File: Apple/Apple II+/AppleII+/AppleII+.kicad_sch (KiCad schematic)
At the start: 0 parts

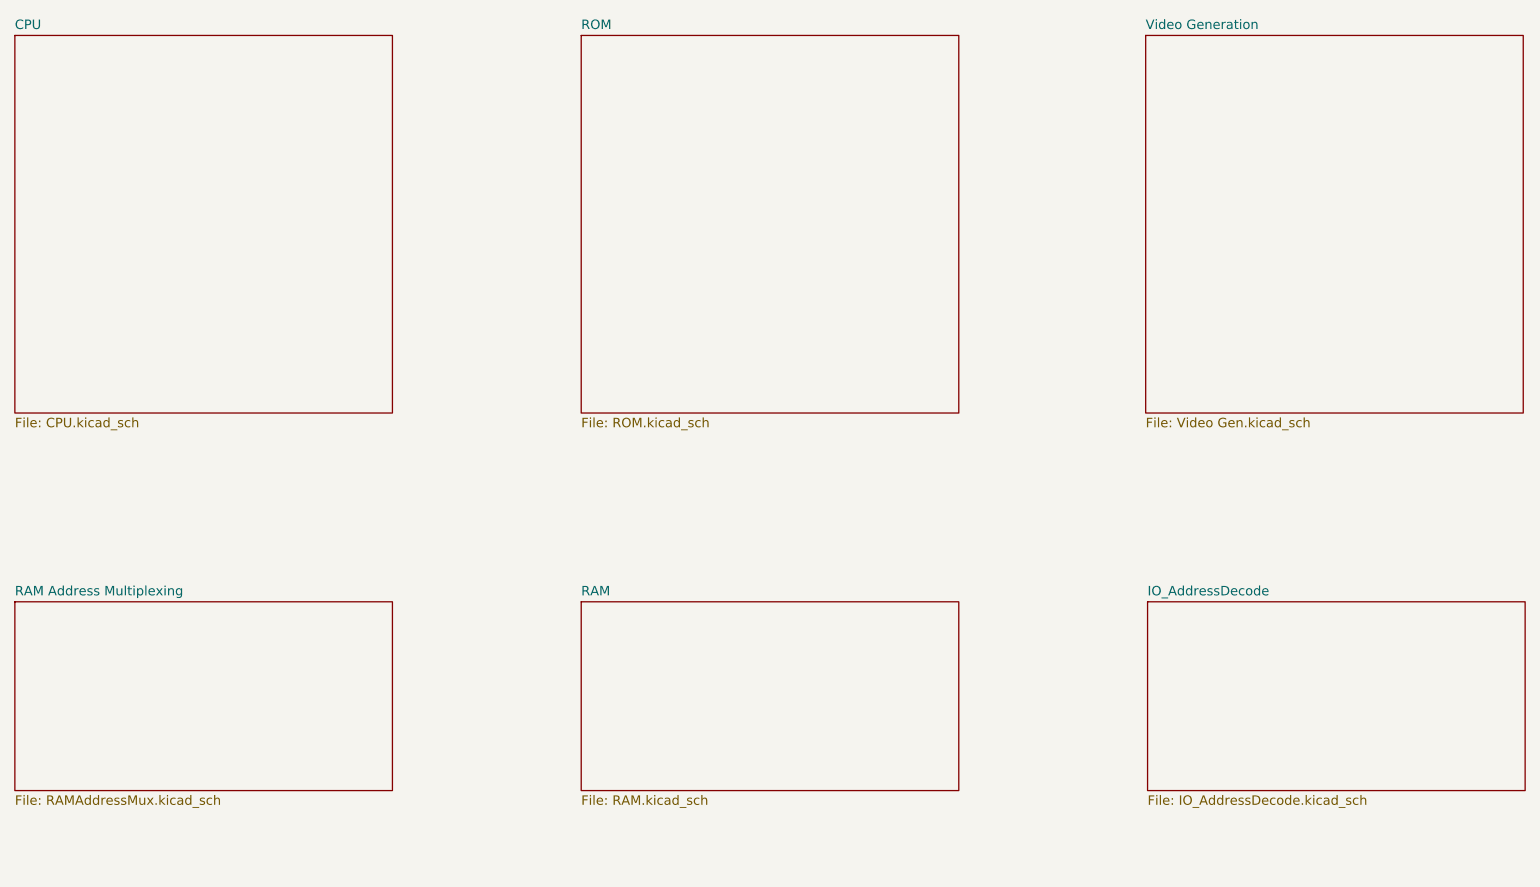
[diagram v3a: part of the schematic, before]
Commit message: Started moving Global labels to Hierarchical and Local labels
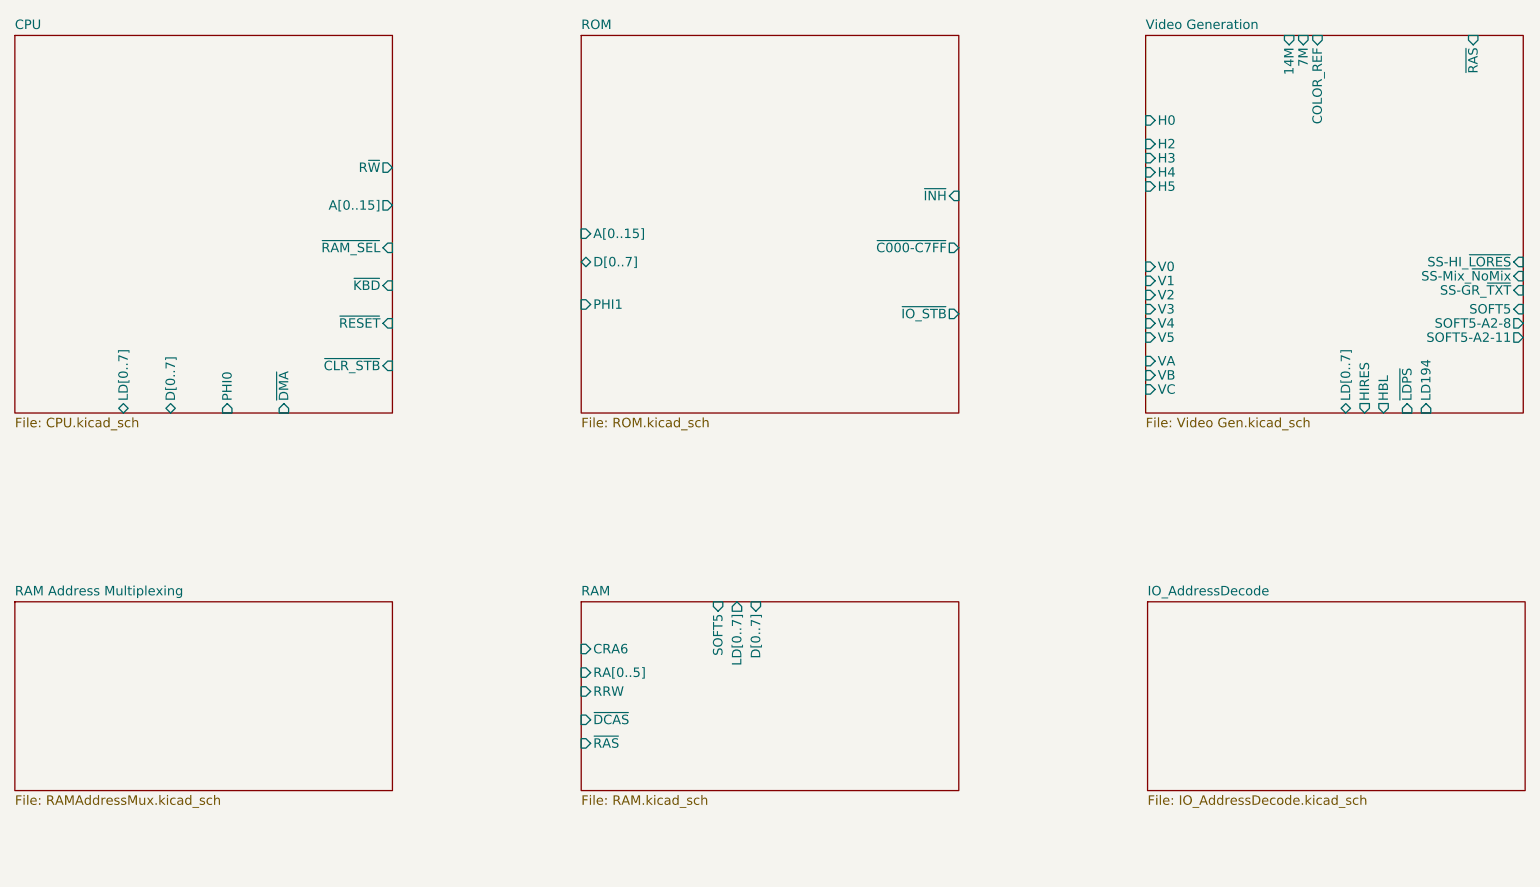
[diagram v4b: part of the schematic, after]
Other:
- sheet CPU ports: added A[0..15], D[0..7], LD[0..7], PHI0, R~{W}, ~{CLR_STB}, ~{DMA}, ~{KBD}, ~{RAM_SEL}, ~{RESET}; removed none
- sheet RAM ports: added CRA6, D[0..7], LD[0..7], RA[0..5], RRW, SOFT5, ~{DCAS}, ~{RAS}; removed none
- sheet ROM ports: added A[0..15], D[0..7], PHI1, ~{C000-C7FF}, ~{INH}, ~{IO_STB}; removed none
- sheet Video Generation ports: added 14M, 7M, COLOR_REF, H0, H2, H3, H4, H5, HBL, HIRES, LD194, LD[0..7], SOFT5, SOFT5-A2-11, SOFT5-A2-8, SS-GR_~{TXT}, SS-HI_~{LORES}, SS-Mix_~{NoMix}, V0, V1, V2, V3, V4, V5, VA, VB, VC, ~{LDPS}, ~{RAS}; removed none
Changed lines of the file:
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@@
       (effects (font (size 1.27 1.27)) (justify left top))
+    )
+    (pin "R~{W}" output (at 76.2 43.18 0)
+      (effects (font (size 1.27 1.27)) (justify right))
+    )
+    (pin "A[0..15]" output (at 76.2 48.26 0)
+      (effects (font (size 1.27 1.27)) (justify right))
+    )
+    (pin "~{RAM_SEL}" input (at 76.2 53.975 0)
+      (effects (font (size 1.27 1.27)) (justify right))
+    )
+    (pin "~{KBD}" input (at 76.2 59.055 0)
+      (effects (font (size 1.27 1.27)) (justify right))
+    )
+    (pin "~{RESET}" input (at 76.2 64.135 0)
+      (effects (font (size 1.27 1.27)) (justify right))
+    )
+    (pin "~{CLR_STB}" input (at 76.2 69.85 0)
+      (effects (font (size 1.27 1.27)) (justify right))
+    )
+    (pin "~{DMA}" input (at 61.595 76.2 270)
+      (effects (font (size 1.27 1.27)) (justify left))
+    )
+    (pin "PHI0" input (at 53.975 76.2 270)
+      (effects (font (size 1.27 1.27)) (justify left))
+    )
+    (pin "D[0..7]" bidirectional (at 46.355 76.2 270)
+      (effects (font (size 1.27 1.27)) (justify left))
+    )
+    (pin "LD[0..7]" bidirectional (at 40.005 76.2 270)
+      (effects (font (size 1.27 1.27)) (justify left))
     )
     (instances
@@
       (effects (font (size 1.27 1.27)) (justify left top))
     )
+    (pin "~{INH}" input (at 152.4 46.99 0)
+      (effects (font (size 1.27 1.27)) (justify right))
+    )
+    (pin "~{C000-C7FF}" output (at 152.4 53.975 0)
+      (effects (font (size 1.27 1.27)) (justify right))
+    )
+    (pin "~{IO_STB}" output (at 152.4 62.865 0)
+      (effects (font (size 1.27 1.27)) (justify right))
+    )
+    (pin "D[0..7]" bidirectional (at 101.6 55.88 180)
+      (effects (font (size 1.27 1.27)) (justify left))
+    )
+    (pin "A[0..15]" input (at 101.6 52.07 180)
+      (effects (font (size 1.27 1.27)) (justify left))
+    )
+    (pin "PHI1" input (at 101.6 61.595 180)
+      (effects (font (size 1.27 1.27)) (justify left))
+    )
     (instances
       (project "AppleII+"
@@
       (effects (font (size 1.27 1.27)) (justify left top))
     )
+    (pin "LD[0..7]" output (at 122.555 101.6 90)
+      (effects (font (size 1.27 1.27)) (justify right))
+    )
+    (pin "CRA6" input (at 101.6 107.95 180)
+      (effects (font (size 1.27 1.27)) (justify left))
+    )
+    (pin "RA[0..5]" input (at 101.6 111.125 180)
+      (effects (font (size 1.27 1.27)) (justify left))
+    )
+    (pin "RRW" input (at 101.6 113.665 180)
+      (effects (font (size 1.27 1.27)) (justify left))
+    )
+    (pin "D[0..7]" input (at 125.095 101.6 90)
+      (effects (font (size 1.27 1.27)) (justify right))
+    )
+    (pin "~{DCAS}" input (at 101.6 117.475 180)
+      (effects (font (size 1.27 1.27)) (justify left))
+    )
+    (pin "~{RAS}" input (at 101.6 120.65 180)
+      (effects (font (size 1.27 1.27)) (justify left))
+    )
+    (pin "SOFT5" input (at 120.015 101.6 90)
+      (effects (font (size 1.27 1.27)) (justify right))
+    )
     (instances
       (project "AppleII+"
@@
       (effects (font (size 1.27 1.27)) (justify left top))
     )
-    (instances
+    (pin "V3" input (at 177.546 62.23 180)
+      (effects (font (size 1.27 1.27)) (justify left))
+    )
+    (pin "V4" input (at 177.546 64.135 180)
+      (effects (font (size 1.27 1.27)) (justify left))
+    )
+    (pin "COLOR_REF" input (at 200.66 25.4 90)
+      (effects (font (size 1.27 1.27)) (justify right))
+    )
+    (pin "H3" input (at 177.546 41.91 180)
+      (effects (font (size 1.27 1.27)) (justify left))
+    )
+    (pin "V5" input (at 177.546 66.04 180)
+      (effects (font (size 1.27 1.27)) (justify left))
+    )
+    (pin "H4" input (at 177.546 43.815 180)
+      (effects (font (size 1.27 1.27)) (justify left))
+    )
+    (pin "H5" input (at 177.546 45.72 180)
+      (effects (font (size 1.27 1.27)) (justify left))
+    )
+    (pin "V1" input (at 177.546 58.42 180)
+      (effects (font (size 1.27 1.27)) (justify left))
+    )
+    (pin "V0" input (at 177.546 56.515 180)
+      (effects (font (size 1.27 1.27)) (justify left))
+    )
+    (pin "VC" input (at 177.546 73.025 180)
+      (effects (font (size 1.27 1.27)) (justify left))
+    )
+    (pin "V2" input (at 177.546 60.325 180)
+      (effects (font (size 1.27 1.27)) (justify left))
+    )
+    (pin "VB" input (at 177.546 71.12 180)
+      (effects (font (size 1.27 1.27)) (justify left))
+    )
+    (pin "VA" input (at 177.546 69.215 180)
+      (effects (font (size 1.27 1.27)) (justify left))
+    )
+    (pin "SOFT5-A2-11" output (at 228.346 66.04 0)
+      (effects (font (size 1.27 1.27)) (justify right))
+    )
+    (pin "SOFT5-A2-8" output (at 228.346 64.135 0)
+      (effects (font (size 1.27 1.27)) (justify right))
+    )
+    (pin "HIRES" output (at 207.01 76.2 270)
+      (effects (font (size 1.27 1.27)) (justify left))
+    )
+    (pin "HBL" output (at 209.55 76.2 270)
+      (effects (font (size 1.27 1.27)) (justify left))
+    )
+    (pin "LD[0..7]" bidirectional (at 204.47 76.2 270)
+      (effects (font (size 1.27 1.27)) (justify left))
+    )
+    (pin "14M" input (at 196.85 25.4 90)
+      (effects (font (size 1.27 1.27)) (justify right))
+    )
+    (pin "7M" input (at 198.755 25.4 90)
+      (effects (font (size 1.27 1.27)) (justify right))
+    )
+    (pin "~{LDPS}" input (at 212.725 76.2 270)
+      (effects (font (size 1.27 1.27)) (justify left))
+    )
+    (pin "LD194" input (at 215.265 76.2 270)
+      (effects (font (size 1.27 1.27)) (justify left))
+    )
+    (pin "SOFT5" input (at 228.346 62.23 0)
+      (effects (font (size 1.27 1.27)) (justify right))
+    )
+    (pin "H0" input (at 177.546 36.83 180)
+      (effects (font (size 1.27 1.27)) (justify left))
+    )
+    (pin "H2" input (at 177.546 40.005 180)
+      (effects (font (size 1.27 1.27)) (justify left))
+    )
+    (pin "SS-GR_~{TXT}" input (at 228.346 59.69 0)
+      (effects (font (size 1.27 1.27)) (justify right))
+    )
+    (pin "SS-Mix_~{NoMix}" input (at 228.346 57.785 0)
+      (effects (font (size 1.27 1.27)) (justify right))
+    )
+    (pin "~{RAS}" input (at 221.615 25.4 90)
+      (effects (font (size 1.27 1.27)) (justify right))
+    )
+    (pin "SS-HI_~{LORES}" input (at 228.346 55.88 0)
+      (effects (font (size 1.27 1.27)) (justify right))
+    )
+    (instances

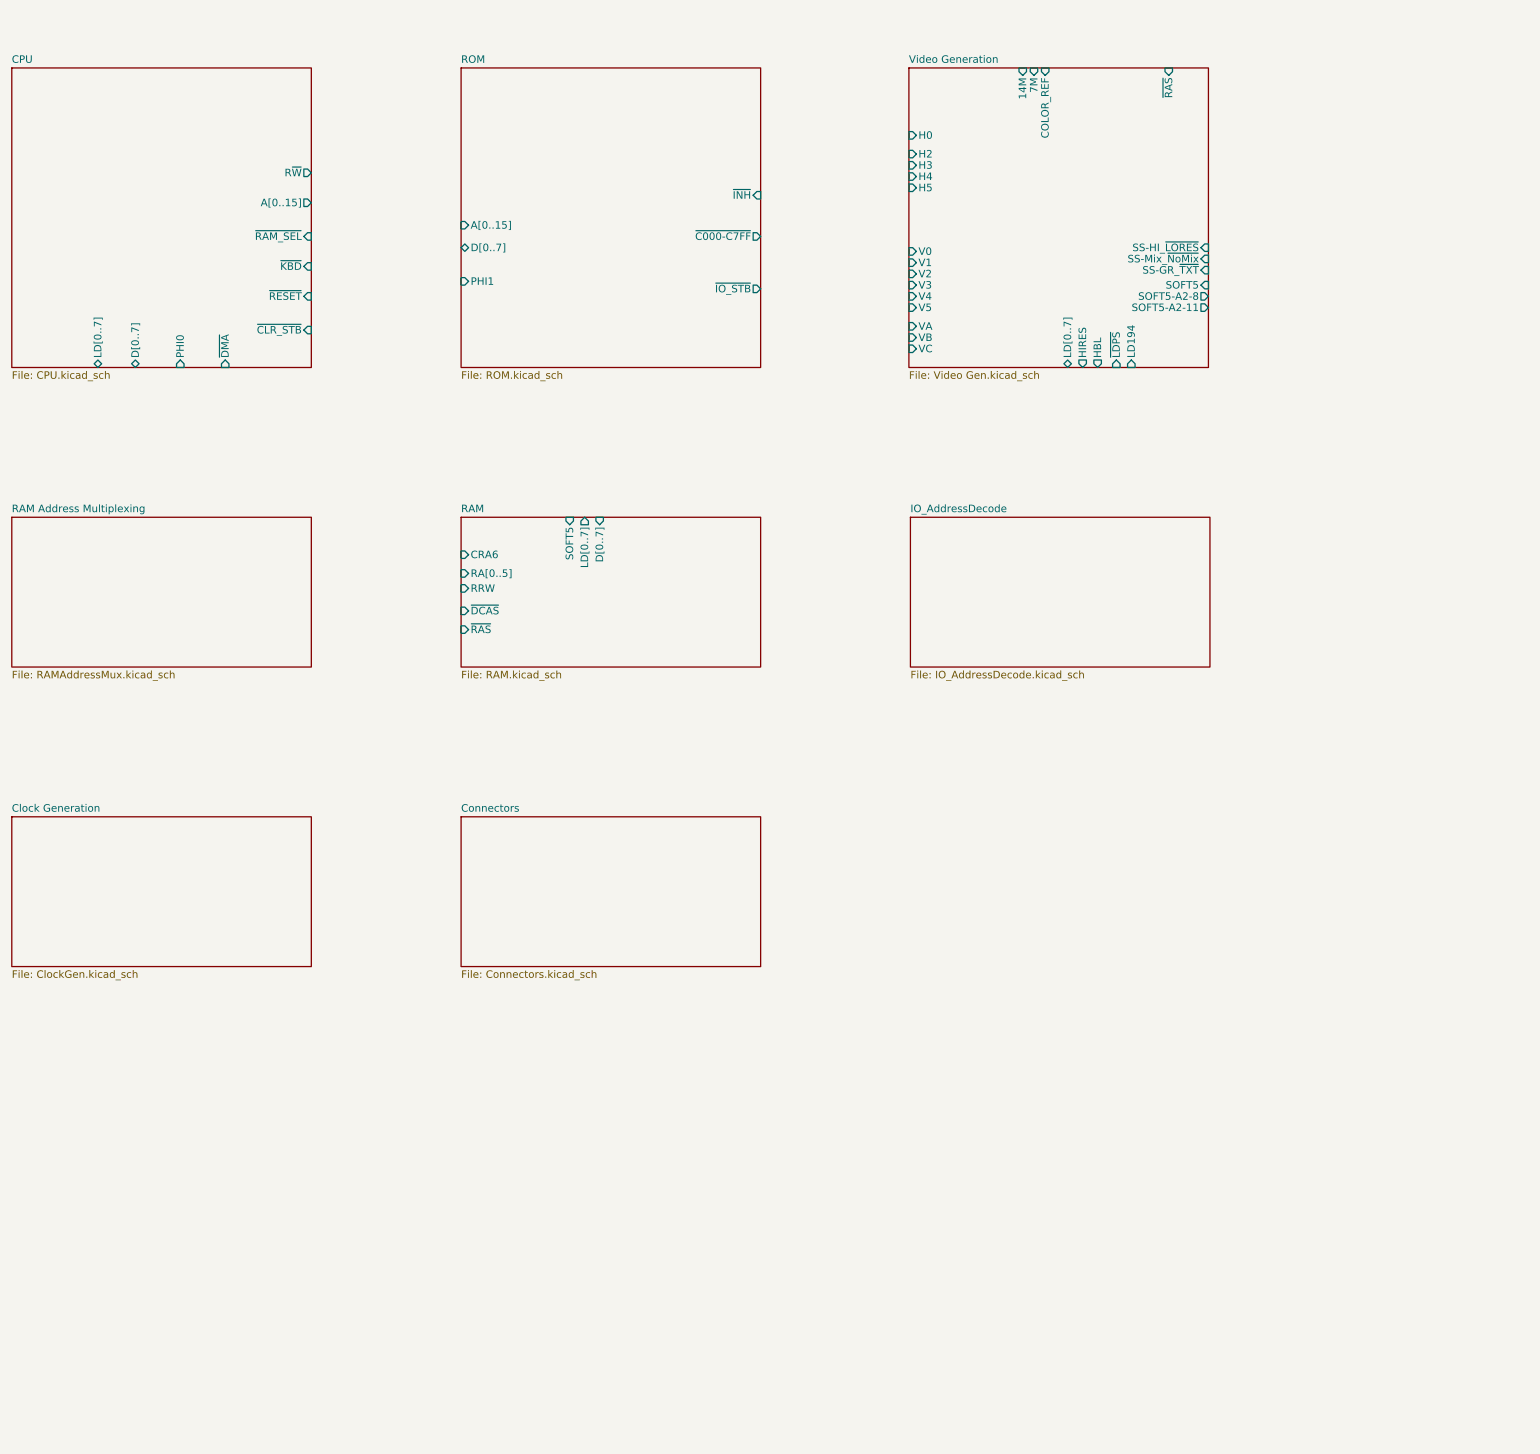
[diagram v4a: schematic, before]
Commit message: Changed global labels to hierachry and started front page changes
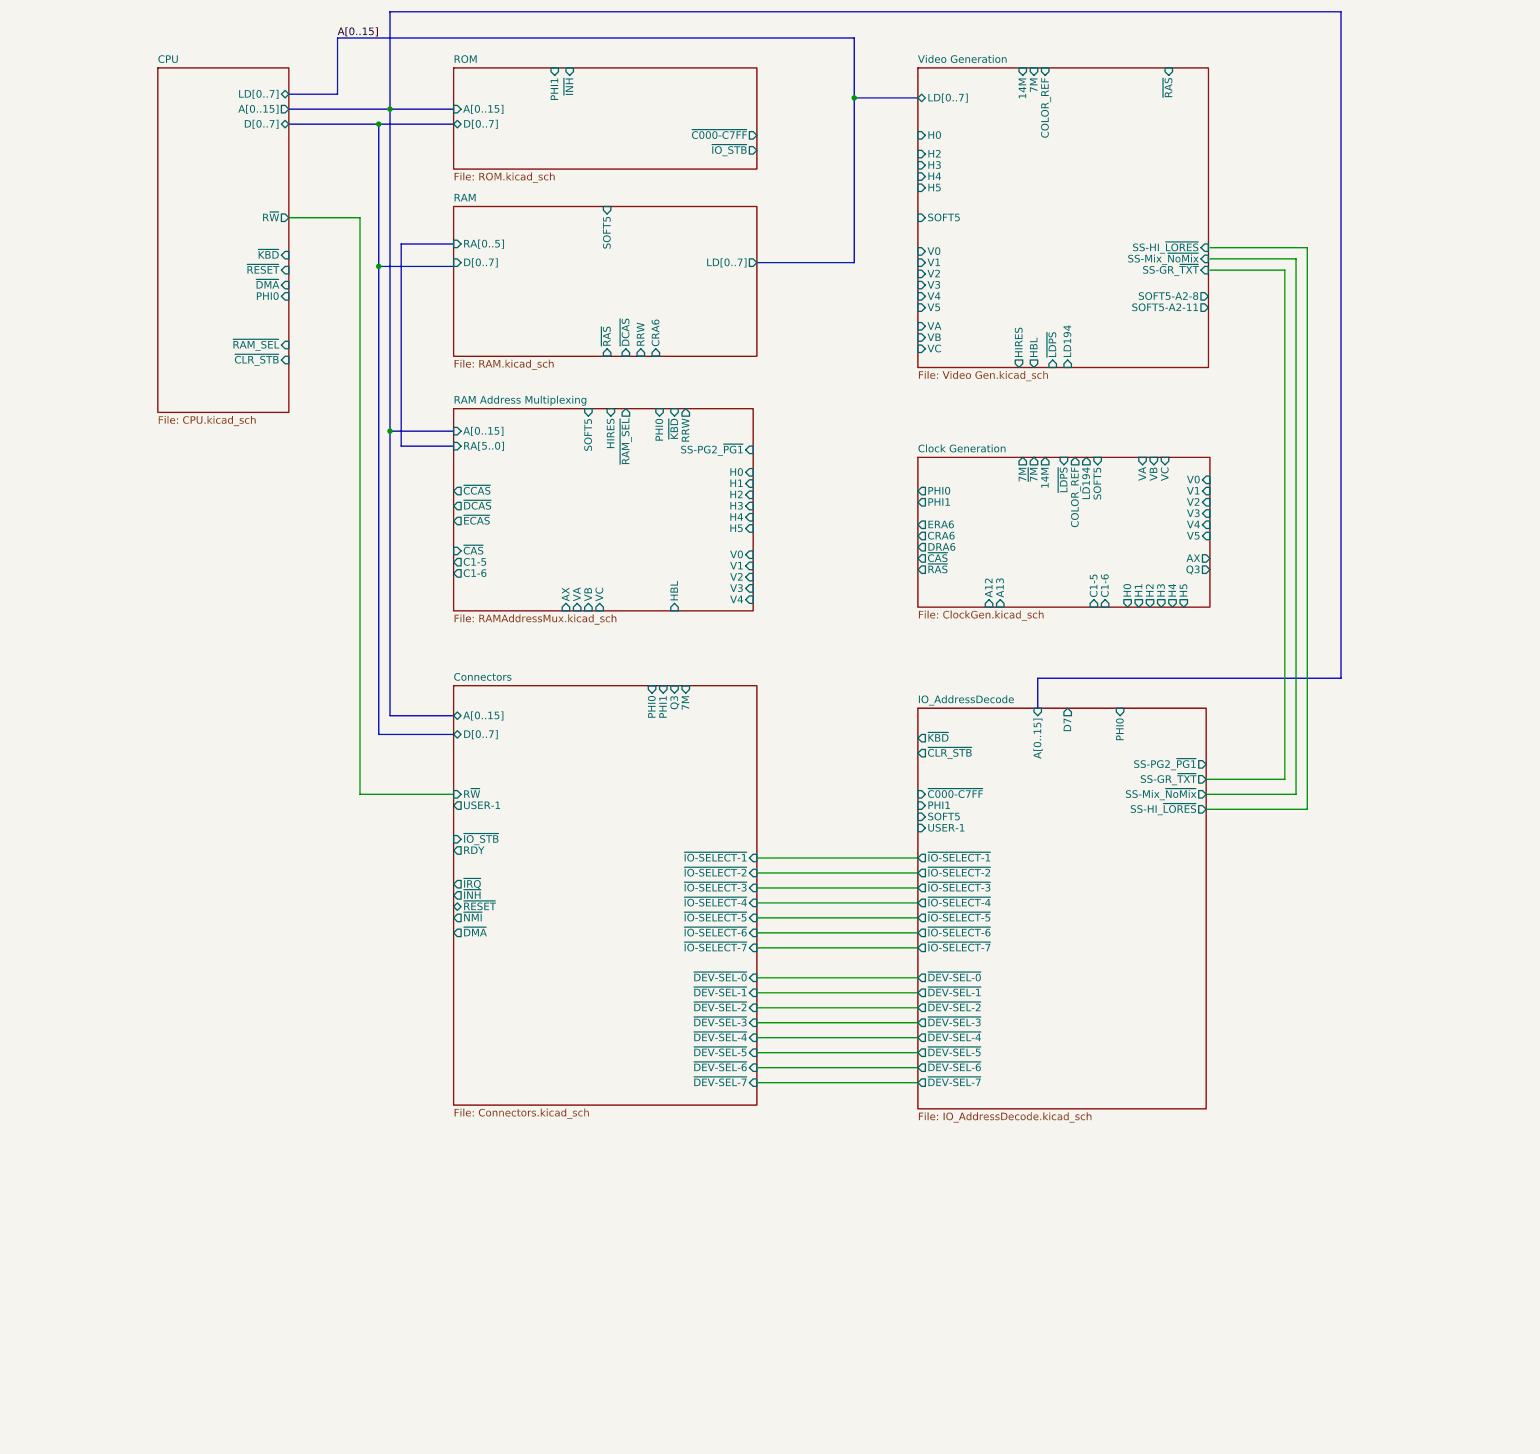
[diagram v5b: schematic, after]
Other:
- sheet Clock Generation ports: added 14M, 7M, A12, A13, AX, C1-5, C1-6, COLOR_REF, CRA6, DRA6, ERA6, H0, H1, H2, H3, H4, H5, LD194, PHI0, PHI1, Q3, SOFT5, V0, V1, V2, V3, V4, V5, VA, VB, VC, ~{7M}, ~{CAS}, ~{LDPS}, ~{RAS}; removed none
- sheet Connectors ports: added 7M, A[0..15], D[0..7], PHI0, PHI1, Q3, RDY, R~{W}, USER-1, ~{DEV-SEL-0}, ~{DEV-SEL-1}, ~{DEV-SEL-2}, ~{DEV-SEL-3}, ~{DEV-SEL-4}, ~{DEV-SEL-5}, ~{DEV-SEL-6}, ~{DEV-SEL-7}, ~{DMA}, ~{INH}, ~{IO-SELECT-1}, ~{IO-SELECT-2}, ~{IO-SELECT-3}, ~{IO-SELECT-4}, ~{IO-SELECT-5}, ~{IO-SELECT-6}, ~{IO-SELECT-7}, ~{IO_STB}, ~{IRQ}, ~{NMI}, ~{RESET}; removed none
- sheet IO_AddressDecode ports: added A[0..15], D7, PHI0, PHI1, SOFT5, SS-GR_~{TXT}, SS-HI_~{LORES}, SS-Mix_~{NoMix}, SS-PG2_~{PG1}, USER-1, ~{C000-C7FF}, ~{CLR_STB}, ~{DEV-SEL-0}, ~{DEV-SEL-1}, ~{DEV-SEL-2}, ~{DEV-SEL-3}, ~{DEV-SEL-4}, ~{DEV-SEL-5}, ~{DEV-SEL-6}, ~{DEV-SEL-7}, ~{IO-SELECT-1}, ~{IO-SELECT-2}, ~{IO-SELECT-3}, ~{IO-SELECT-4}, ~{IO-SELECT-5}, ~{IO-SELECT-6}, ~{IO-SELECT-7}, ~{KBD}; removed none
- sheet RAM Address Multiplexing ports: added AX, A[0..15], C1-5, C1-6, H0, H1, H2, H3, H4, H5, HBL, HIRES, PHI0, RA[5..0], RRW, SOFT5, SS-PG2_~{PG1}, V0, V1, V2, V3, V4, VA, VB, VC, ~{CAS}, ~{CCAS}, ~{DCAS}, ~{ECAS}, ~{KBD}, ~{RAM_SEL}; removed none
